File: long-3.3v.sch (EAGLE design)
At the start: 35 parts, among them U1 USD-SOCKET, U2 MCP73831, U4 ADXL375BCCZ, X1 Micro USB, X2 CRYSTAL

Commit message: Updated schematic, unrouted board Added temperature sensor, power switch, 32.768kHz crystal Changed 8MHz crystal Changed connections to micro
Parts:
- removed JP11, JP12, JP13: (no value), SparkFun-Connectors:M06SIP
- added C12, C13: 20pF, rcl:C-EUC0402
- added C14: 100nF, rcl:C-EUC0402
- added J1: CON_HEADER_1X06-SMD-RIGHT-ANGLED, dp_devices:CON_HEADER_1X06-SMD-RIGHT-ANGLED
- added JP1, JP2: (no value), SparkFun:M05PTH
- added JP3, JP4: (no value), SparkFun:M07
- added Q1: BSS84, transistor-small-signal:BSS84
- added R6: 0R, SparkFun:RESISTOR0402-RES
- added R7: 100k, SparkFun:RESISTOR0402-RES
- added U3: MCP9808T-E/MC, mattsLib:MCP9808T-E/MC
- added X3: CRYSTALS-NOGND-IQXC-25, IQD-Frequency-Products:CRYSTALS-NOGND-IQXC-25
- R1: value 10k -> 100k
- X2: device IQD-Frequency-Products:CRYSTALS-NOGND-12SMX-B -> Ava:ABRACON_ABM3_CRYSTAL; OC_FARNELL 1276690 -> 2101329
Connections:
- removed net CS: U$1.PA15
- removed net FC_RX: U$1.PA10
- removed net FC_TX: U$1.PA9
- removed net MISO: U$1.PB4
- removed net MOSI: U$1.PB5
- removed net PA0: JP11.6, U$1.PA0
- removed net PA1: JP11.5, U$1.PA1
- removed net PB0: U$1.PB0
- removed net PB1: U$1.PB1
- removed net RX: JP11.2, U$1.PA3
- removed net RX2: JP14.1
- removed net SCK: U$1.PB3
- removed net SCL: JP11.4, R2.2, U$1.PB6, U4.SCL/SCLK
- removed net SDA: JP11.3, R5.2, U$1.PB7, U4.SDA/SDI/SDIO
- removed net SPI_CS: JP13.1
- removed net SPI_MISO: JP13.3
- removed net SPI_MOSI: JP13.4
- removed net SPI_SCK: JP13.2
- removed net TX: JP11.1, U$1.PA2
- removed net TX2: JP14.2
- removed net VIN: C3.1, R3.2, U2.VIN, X1.VBUS
- new net BOOT0: R6.1, U$1.BOOT0
- new net EXT_CS: JP1.5, JP2.5, U$1.PA4
- new net EXT_MISO: JP1.3, JP2.3, U$1.PB4
- new net EXT_MOSI: JP1.2, JP2.2, U$1.PB5
- new net EXT_RX: JP3.6, U$1.PA3
- new net EXT_SCK: JP1.4, JP2.4, U$1.PB12
- new net EXT_SW: Q1.G, R7.2, U$1.PC13
- new net EXT_TX: JP3.7, U$1.PA2
- new net LOCAL_SCL: U$1.PB10, U3.SCL
- new net LOCAL_SDA: U$1.PB3, U3.SDA
- new net N$6: C13.1, U$1.PC15-OSC32_OUT, X3.2
- new net N$7: C12.1, U$1.PC14-OSC32_IN, X3.1
- new net RADIO_DATA: U$1.PA8, U$3.P$4
- new net VBUS: C3.1, R3.2, U$1.PA9, U2.VIN, X1.VBUS
- new net VCC_SW: JP15.1, JP17.1, Q1.D
- net GND: now also C12.2, C13.2, C14.2, J1.3, R6.2, U$1.VSSA/VREF-, U1.CD2, U3.EPAD, U3.GND
- net GPIO1: now also JP3.1, JP4.1, U$1.PA0; no longer JP12.6
- net GPIO2: now also JP3.2, JP4.2, U$1.PA1; no longer JP12.5
- net GPIO3: now also JP3.3, JP4.3, U$1.PB0; no longer JP13.6
- net GPIO4: now also JP1.1, JP2.1, U$1.PB1; no longer JP13.5
- net GPS_RX: now also JP14.2, U$1.PB6
- net GPS_TX: now also JP14.1, U$1.PA10
- net I2C_SCL: now also JP3.4, JP4.4, R2.2, U$1.PB8, U4.SCL/SCLK; no longer JP12.4
- net I2C_SDA: now also JP3.5, JP4.5, R5.2, U$1.PB7, U4.SDA/SDI/SDIO; no longer JP12.3
- net NRST: now also J1.5
- net RADIO_CS: now also U$1.PB9; no longer U$1.PB12
- net SD_CS: now also U$1.PA15; no longer U$1.PA4
- net SWCLK: now also J1.2
- net SWDIO: now also J1.4
- net UART_RX: now also JP4.6; no longer JP12.2
- net UART_TX: now also JP4.7; no longer JP12.1
- net VCC: now also C14.1, J1.1, Q1.S, R7.1, U$1.VBAT, U$1.VDDA/VREF+, U3.A0, U3.A1, U3.A2, U3.VDD; no longer JP15.1, JP17.1
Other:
- moved on the sheet: C1, C2, C7, C9, JP15, JP16, JP17, U4, X2

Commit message: Routed all the things (main board)
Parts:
- removed R6: 0R, SparkFun:RESISTOR0402-RES
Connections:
- removed net BOOT0: R6.1, U$1.BOOT0
- net EXT_CS: now also U$1.PA15; no longer U$1.PA4
- net EXT_SCK: now also U$1.PB3; no longer U$1.PB12
- net GND: now also U$1.BOOT0; no longer R6.2
- net I2C_SCL: now also U$1.PB10; no longer U$1.PB8
- net I2C_SDA: now also U$1.PB9; no longer U$1.PB7
- net LOCAL_SCL: now also U$1.PB8; no longer U$1.PB10
- net LOCAL_SDA: now also U$1.PB7; no longer U$1.PB3
- net RADIO_CS: now also U$1.PB12; no longer U$1.PB9
- net SD_CS: now also U$1.PA4; no longer U$1.PA15
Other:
- moved on the sheet: C14, C8, C9, U1, U3

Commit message: Switched from SD card to Flash memory
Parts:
- removed U1: USD-SOCKET, SparkFun-Connectors:USD-SOCKET
- added U$5: S25FL256, mattsLib:S25FL256
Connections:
- removed net SD_CS: U$1.PA4, U1.CS
- removed net SD_MISO: U$1.PA6, U1.DO
- removed net SD_MOSI: U$1.PA7, U1.DI
- removed net SD_SCK: U$1.PA5, U1.SCK
- new net FLASH_CS: U$1.PA4, U$5.CS#
- new net FLASH_MISO: U$1.PA6, U$5.SO/IO1
- new net FLASH_MOSI: U$1.PA7, U$5.SI/IO0
- new net FLASH_SCK: U$1.PA5, U$5.SCK
- net GND: now also U$5.PAD, U$5.VSS; no longer U1.CD2, U1.GND, U1.SHIELD@1, U1.SHIELD@3
- net VCC: now also U$5.VCC; no longer U1.VCC
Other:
- moved on the sheet: C14, C8, C9, U3

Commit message: Changed layout, routed board
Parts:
- removed JP14, JP15, JP16, JP17: M02PTH, SparkFun-Connectors:M02PTH
- removed U$2: UBLOX_MAX, Ava:UBLOX_MAX
- removed U4: ADXL375BCCZ, adxl375bccz:ADXL375BCCZ
- added C15: 100nF, rcl:C-EUC0402
- added R6, R8: 3k3, SparkFun:RESISTOR0402-RES
- JP1, JP2: device SparkFun:M05PTH -> SparkFun:M03PTH
- JP3, JP4: device SparkFun:M07 -> SparkFun:M05PTH
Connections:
- removed net UART_RX: JP4.6
- removed net UART_TX: JP4.7
- net EXT_CS: now also JP4.3; no longer JP1.5, JP2.5
- net EXT_MISO: now also JP4.4; no longer JP1.3, JP2.3
- net EXT_MOSI: now also JP4.2; no longer JP1.2, JP2.2
- net EXT_RX: now also JP2.2; no longer JP3.6
- net EXT_SCK: now also JP4.5; no longer JP1.4, JP2.4
- net EXT_TX: now also JP2.3; no longer JP3.7
- net GND: now also C15.2, JP1.3; no longer JP15.2, JP17.2, U$2.10_GND, U$2.12_GND, U$2.1_GND, U4.GND, U4.GND_2, U4.GND_3
- net GPIO1: no longer JP4.1
- net GPIO2: no longer JP4.2
- net GPIO3: no longer JP4.3
- net GPIO4: now also JP3.4; no longer JP1.1, JP2.1
- net GPS_RX: now also JP4.1; no longer JP14.2, JP16.2, U$2.3_RXD1
- net GPS_TX: now also JP3.5; no longer JP14.1, JP16.1, U$2.2_TXD1
- net I2C_SCL: now also JP1.1; no longer JP3.4, JP4.4, U4.SCL/SCLK
- net I2C_SDA: now also JP2.1; no longer JP3.5, JP4.5, U4.SDA/SDI/SDIO
- net LOCAL_SCL: now also R8.2
- net LOCAL_SDA: now also R6.2
- net VCC: now also C15.1, R6.1, R8.1; no longer U$2.14_VCC_RF, U$2.6_V_BCKP, U$2.7_VCC_IO, U$2.8_VCC, U$2.9_V_RESET, U4.VDD_I/O, U4.VS
- net VCC_SW: now also JP1.2; no longer JP15.1, JP17.1

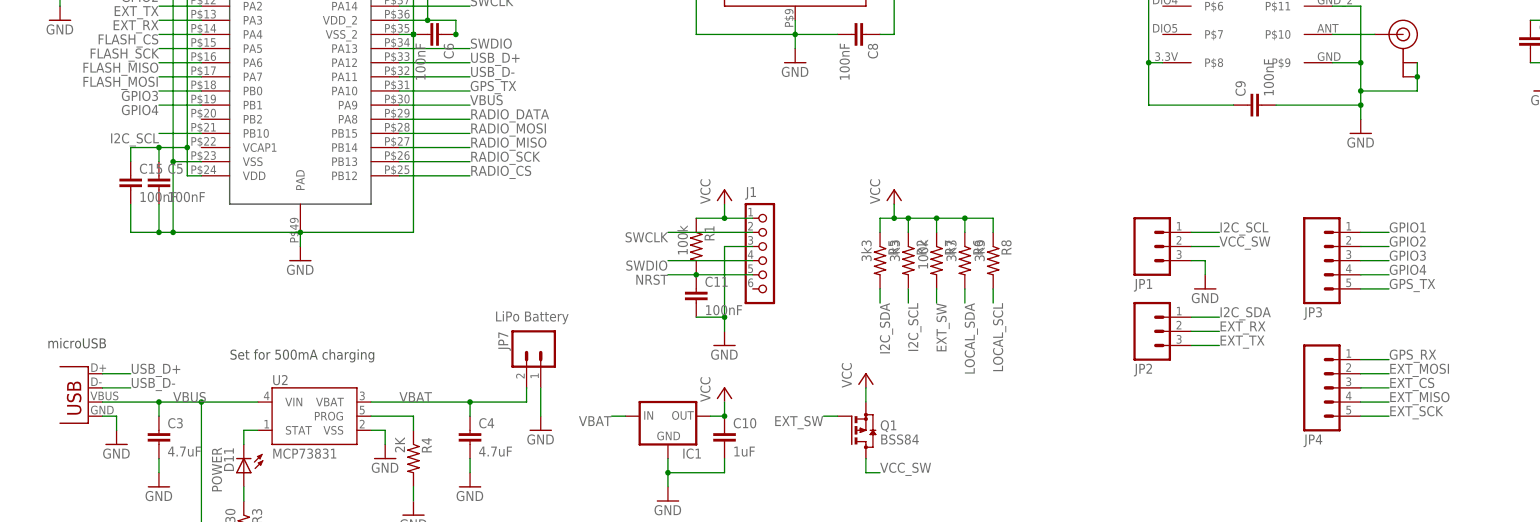
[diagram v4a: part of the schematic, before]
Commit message: New layout routed
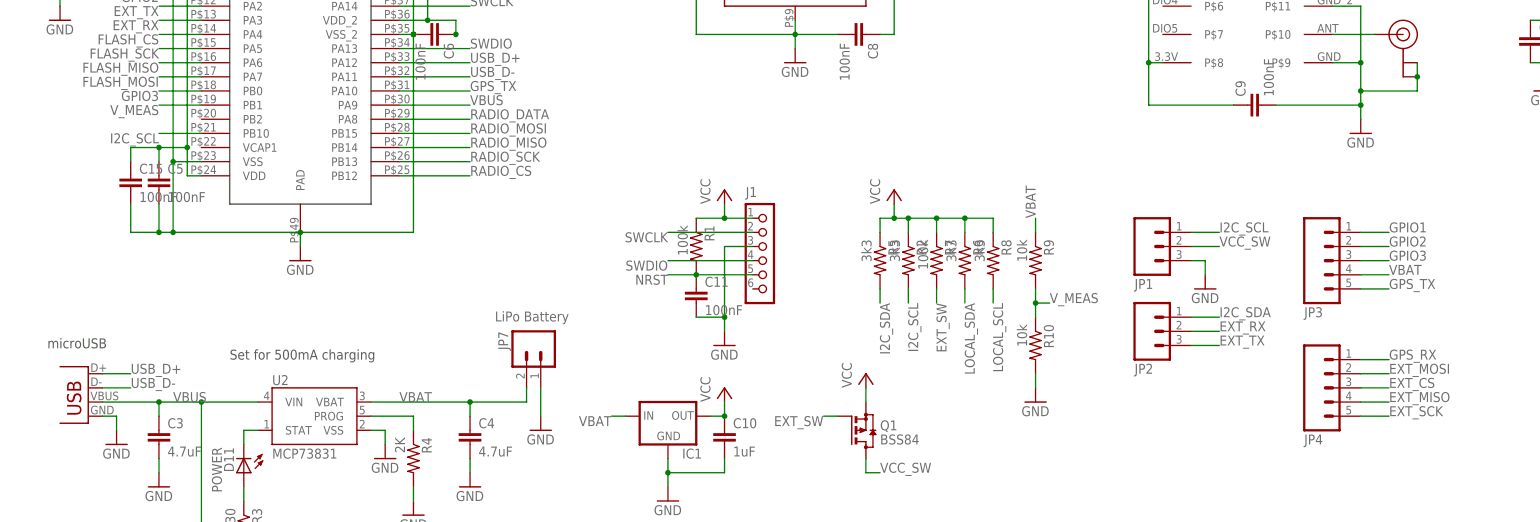
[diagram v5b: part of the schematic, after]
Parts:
- added R10, R9: 10k, SparkFun:RESISTOR0402-RES
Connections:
- removed net GPIO4: JP3.4, U$1.PB1
- new net V_MEAS: R10.1, R9.2, U$1.PB1
- net GND: now also R10.2
- net VBAT: now also JP3.4, R9.1
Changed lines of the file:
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@@
 <part name="R8" library="SparkFun" deviceset="RESISTOR" device="0402-RES" value="3k3"/>
 <part name="C15" library="rcl" deviceset="C-EU" device="C0402" value="100nF"/>
+<part name="R9" library="SparkFun" deviceset="RESISTOR" device="0402-RES" value="10k"/>
+<part name="R10" library="SparkFun" deviceset="RESISTOR" device="0402-RES" value="10k"/>
+<part name="GND6" library="supply1" deviceset="GND" device=""/>
 </parts>
 <sheets>
@@
 <instance part="R8" gate="G$1" x="177.8" y="66.04" rot="R270"/>
 <instance part="C15" gate="G$1" x="22.86" y="81.28"/>
+<instance part="R9" gate="G$1" x="185.42" y="66.04" rot="R270"/>
+<instance part="R10" gate="G$1" x="185.42" y="50.8" rot="R270"/>
+<instance part="GND6" gate="1" x="185.42" y="40.64"/>
 </instances>
 <busses>
@@
 <wire x1="215.9" y1="66.04" x2="213.36" y2="66.04" width="0.1524" layer="91"/>
 </segment>
+<segment>
+<pinref part="GND6" gate="1" pin="GND"/>
+<pinref part="R10" gate="G$1" pin="2"/>
+<wire x1="185.42" y1="43.18" x2="185.42" y2="45.72" width="0.1524" layer="91"/>
+</segment>
 </net>
 <net name="VBAT" class="0">
@@
 <wire x1="111.76" y1="38.1" x2="109.22" y2="38.1" width="0.1524" layer="91"/>
 <label x="109.22" y="38.1" size="1.778" layer="95" rot="R180"/>
+</segment>
+<segment>
+<pinref part="R9" gate="G$1" pin="1"/>
+<wire x1="185.42" y1="71.12" x2="185.42" y2="73.66" width="0.1524" layer="91"/>
+<label x="185.42" y="73.66" size="1.778" layer="95" rot="R90"/>
+</segment>
+<segment>
+<pinref part="JP3" gate="G$1" pin="4"/>
+<wire x1="243.84" y1="63.5" x2="248.92" y2="63.5" width="0.1524" layer="91"/>
+<label x="248.92" y="63.5" size="1.778" layer="95"/>
 </segment>
 </net>
@@
 </segment>
 </net>
-<net name="GPIO4" class="0">
-<segment>
-<pinref part="U$1" gate="G$1" pin="PB1"/>
-<wire x1="35.56" y1="93.98" x2="27.94" y2="93.98" width="0.1524" layer="91"/>
-<label x="27.94" y="93.98" size="1.778" layer="95" rot="R180"/>
-</segment>
-<segment>
-<pinref part="JP3" gate="G$1" pin="4"/>
-<wire x1="243.84" y1="63.5" x2="248.92" y2="63.5" width="0.1524" layer="91"/>
-<label x="248.92" y="63.5" size="1.778" layer="95"/>
-</segment>
-</net>
 <net name="I2C_SDA" class="0">
 <segment>
@@
 </segment>
 </net>
+<net name="V_MEAS" class="0">
+<segment>
+<pinref part="U$1" gate="G$1" pin="PB1"/>
+<wire x1="35.56" y1="93.98" x2="27.94" y2="93.98" width="0.1524" layer="91"/>
+<label x="27.94" y="93.98" size="1.778" layer="95" rot="R180"/>
+</segment>
+<segment>
+<pinref part="R10" gate="G$1" pin="1"/>
+<pinref part="R9" gate="G$1" pin="2"/>
+<wire x1="185.42" y1="55.88" x2="185.42" y2="58.42" width="0.1524" layer="91"/>
+<wire x1="185.42" y1="58.42" x2="185.42" y2="60.96" width="0.1524" layer="91"/>
+<wire x1="185.42" y1="58.42" x2="187.96" y2="58.42" width="0.1524" layer="91"/>
+<junction x="185.42" y="58.42"/>
+<label x="187.96" y="58.42" size="1.778" layer="95"/>
+</segment>
+</net>

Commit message: updated RF
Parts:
- added C16, C17: (no value), rcl:C-EUC0402
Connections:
- new net N$5: C16.1, C17.2, U$3.P$10
- net GND: now also C17.1
- net N$4: now also C16.2; no longer U$3.P$10
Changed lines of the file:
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@@
 <grid distance="0.1" unitdist="inch" unit="inch" style="lines" multiple="1" display="no" altdistance="0.01" altunitdist="inch" altunit="inch"/>
 <layers>
-<layer number="1" name="Top" color="4" fill="1" visible="yes" active="no"/>
-<layer number="16" name="Bottom" color="1" fill="1" visible="yes" active="no"/>
-<layer number="17" name="Pads" color="2" fill="1" visible="yes" active="no"/>
-<layer number="18" name="Vias" color="2" fill="1" visible="yes" active="no"/>
-<layer number="19" name="Unrouted" color="6" fill="1" visible="yes" active="no"/>
-<layer number="20" name="Dimension" color="15" fill="1" visible="yes" active="no"/>
-<layer number="21" name="tPlace" color="7" fill="1" visible="yes" active="no"/>
-<layer number="22" name="bPlace" color="7" fill="1" visible="yes" active="no"/>
-<layer number="23" name="tOrigins" color="15" fill="1" visible="yes" active="no"/>
-<layer number="24" name="bOrigins" color="15" fill="1" visible="yes" active="no"/>
-<layer number="25" name="tNames" color="7" fill="1" visible="yes" active="no"/>
-<layer number="26" name="bNames" color="7" fill="1" visible="yes" active="no"/>
-<layer number="27" name="tValues" color="7" fill="1" visible="yes" active="no"/>
-<layer number="28" name="bValues" color="7" fill="1" visible="yes" active="no"/>
+<layer number="1" name="Top" color="4" fill="1" visible="no" active="no"/>
+<layer number="16" name="Bottom" color="1" fill="1" visible="no" active="no"/>
+<layer number="17" name="Pads" color="2" fill="1" visible="no" active="no"/>
+<layer number="18" name="Vias" color="2" fill="1" visible="no" active="no"/>
+<layer number="19" name="Unrouted" color="6" fill="1" visible="no" active="no"/>
+<layer number="20" name="Dimension" color="15" fill="1" visible="no" active="no"/>
+<layer number="21" name="tPlace" color="7" fill="1" visible="no" active="no"/>
+<layer number="22" name="bPlace" color="7" fill="1" visible="no" active="no"/>
+<layer number="23" name="tOrigins" color="15" fill="1" visible="no" active="no"/>
+<layer number="24" name="bOrigins" color="15" fill="1" visible="no" active="no"/>
+<layer number="25" name="tNames" color="7" fill="1" visible="no" active="no"/>
+<layer number="26" name="bNames" color="7" fill="1" visible="no" active="no"/>
+<layer number="27" name="tValues" color="7" fill="1" visible="no" active="no"/>
+<layer number="28" name="bValues" color="7" fill="1" visible="no" active="no"/>
 <layer number="29" name="tStop" color="7" fill="3" visible="no" active="no"/>
 <layer number="30" name="bStop" color="7" fill="6" visible="no" active="no"/>
@@
 <layer number="35" name="tGlue" color="7" fill="4" visible="no" active="no"/>
 <layer number="36" name="bGlue" color="7" fill="5" visible="no" active="no"/>
-<layer number="37" name="tTest" color="7" fill="1" visible="yes" active="no"/>
-<layer number="38" name="bTest" color="7" fill="1" visible="yes" active="no"/>
+<layer number="37" name="tTest" color="7" fill="1" visible="no" active="no"/>
+<layer number="38" name="bTest" color="7" fill="1" visible="no" active="no"/>
 <layer number="39" name="tKeepout" color="4" fill="11" visible="no" active="no"/>
 <layer number="40" name="bKeepout" color="1" fill="11" visible="no" active="no"/>
@@
 <layer number="44" name="Drills" color="7" fill="1" visible="no" active="no"/>
 <layer number="45" name="Holes" color="7" fill="1" visible="no" active="no"/>
-<layer number="46" name="Milling" color="3" fill="1" visible="yes" active="no"/>
-<layer number="47" name="Measures" color="7" fill="1" visible="yes" active="no"/>
-<layer number="48" name="Document" color="7" fill="1" visible="yes" active="no"/>
-<layer number="49" name="Reference" color="7" fill="1" visible="yes" active="no"/>
-<layer number="50" name="dxf" color="7" fill="1" visible="yes" active="no"/>
-<layer number="51" name="tDocu" color="7" fill="1" visible="yes" active="no"/>
-<layer number="52" name="bDocu" color="7" fill="1" visible="yes" active="no"/>
-<layer number="53" name="tGND_GNDA" color="7" fill="9" visible="yes" active="no"/>
-<layer number="54" name="bGND_GNDA" color="1" fill="9" visible="yes" active="no"/>
-<layer number="56" name="wert" color="7" fill="1" visible="yes" active="no"/>
-<layer number="57" name="tCAD" color="7" fill="1" visible="yes" active="no"/>
+<layer number="46" name="Milling" color="3" fill="1" visible="no" active="no"/>
+<layer number="47" name="Measures" color="7" fill="1" visible="no" active="no"/>
+<layer number="48" name="Document" color="7" fill="1" visible="no" active="no"/>
+<layer number="49" name="Reference" color="7" fill="1" visible="no" active="no"/>
+<layer number="50" name="dxf" color="7" fill="1" visible="no" active="no"/>
+<layer number="51" name="tDocu" color="7" fill="1" visible="no" active="no"/>
+<layer number="52" name="bDocu" color="7" fill="1" visible="no" active="no"/>
+<layer number="53" name="tGND_GNDA" color="7" fill="9" visible="no" active="no"/>
+<layer number="54" name="bGND_GNDA" color="1" fill="9" visible="no" active="no"/>
+<layer number="56" name="wert" color="7" fill="1" visible="no" active="no"/>
+<layer number="57" name="tCAD" color="7" fill="1" visible="no" active="no"/>
 <layer number="90" name="Modules" color="5" fill="1" visible="yes" active="yes"/>
 <layer number="91" name="Nets" color="2" fill="1" visible="yes" active="yes"/>
@@
 <part name="R10" library="SparkFun" deviceset="RESISTOR" device="0402-RES" value="10k"/>
 <part name="GND6" library="supply1" deviceset="GND" device=""/>
+<part name="C16" library="rcl" deviceset="C-EU" device="C0402"/>
+<part name="C17" library="rcl" deviceset="C-EU" device="C0402"/>
 </parts>
 <sheets>
@@
 <instance part="R5" gate="G$1" x="157.48" y="66.04" rot="R270"/>
 <instance part="P+11" gate="VCC" x="160.02" y="78.74"/>
-<instance part="U$4" gate="G$1" x="251.46" y="106.68" rot="MR0"/>
+<instance part="U$4" gate="G$1" x="259.08" y="106.68" rot="MR0"/>
 <instance part="X3" gate="G$1" x="-10.16" y="127" smashed="yes">
 <attribute name="OC_FARNELL" x="-10.16" y="127" size="1.778" layer="96" display="off"/>
@@
 <instance part="R10" gate="G$1" x="185.42" y="50.8" rot="R270"/>
 <instance part="GND6" gate="1" x="185.42" y="40.64"/>
+<instance part="C16" gate="G$1" x="248.92" y="106.68" rot="R90"/>
+<instance part="C17" gate="G$1" x="246.38" y="101.6" rot="R180"/>
 </instances>
 <busses>
@@
 <pinref part="U$4" gate="G$1" pin="GND@0"/>
 <pinref part="U$4" gate="G$1" pin="GND@1"/>
-<wire x1="254" y1="101.6" x2="254" y2="99.06" width="0.1524" layer="91"/>
-<wire x1="254" y1="99.06" x2="254" y2="96.52" width="0.1524" layer="91"/>
-<wire x1="254" y1="96.52" x2="243.84" y2="96.52" width="0.1524" layer="91"/>
-<junction x="254" y="99.06"/>
+<wire x1="261.62" y1="101.6" x2="261.62" y2="99.06" width="0.1524" layer="91"/>
+<wire x1="261.62" y1="99.06" x2="261.62" y2="96.52" width="0.1524" layer="91"/>
+<wire x1="261.62" y1="96.52" x2="246.38" y2="96.52" width="0.1524" layer="91"/>
+<junction x="261.62" y="99.06"/>
 <junction x="243.84" y="96.52"/>
+<pinref part="C17" gate="G$1" pin="1"/>
+<wire x1="246.38" y1="96.52" x2="243.84" y2="96.52" width="0.1524" layer="91"/>
+<wire x1="246.38" y1="99.06" x2="246.38" y2="96.52" width="0.1524" layer="91"/>
+<junction x="246.38" y="96.52"/>
 </segment>
 <segment>
@@
 </segment>
 </net>
-<net name="N$4" class="0">
-<segment>
-<pinref part="U$4" gate="G$1" pin="SIGNAL"/>
-<pinref part="U$3" gate="G$1" pin="P$10"/>
-<wire x1="246.38" y1="106.68" x2="238.76" y2="106.68" width="0.1524" layer="91"/>
-</segment>
-</net>
 <net name="EXT_CS" class="0">
 <segment>
@@
 </segment>
 </net>
+<net name="N$4" class="0">
+<segment>
+<pinref part="U$4" gate="G$1" pin="SIGNAL"/>
+<pinref part="C16" gate="G$1" pin="2"/>
+</segment>
+</net>
+<net name="N$5" class="0">
+<segment>
+<pinref part="C16" gate="G$1" pin="1"/>
+<pinref part="C17" gate="G$1" pin="2"/>
+<pinref part="U$3" gate="G$1" pin="P$10"/>
+<wire x1="238.76" y1="106.68" x2="246.38" y2="106.68" width="0.1524" layer="91"/>
+<junction x="246.38" y="106.68"/>
+</segment>
+</net>
